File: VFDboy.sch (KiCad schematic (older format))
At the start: 59 parts, among them J1 AVR-ISP-6, SW1 RIGHT, SW2 A, SW3 DOWN, SW4 UP, SW5 LEFT, SW6 B, U1 ATmega32U4-MU, U2 SSD1306_VFD, U7 SRV05-4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

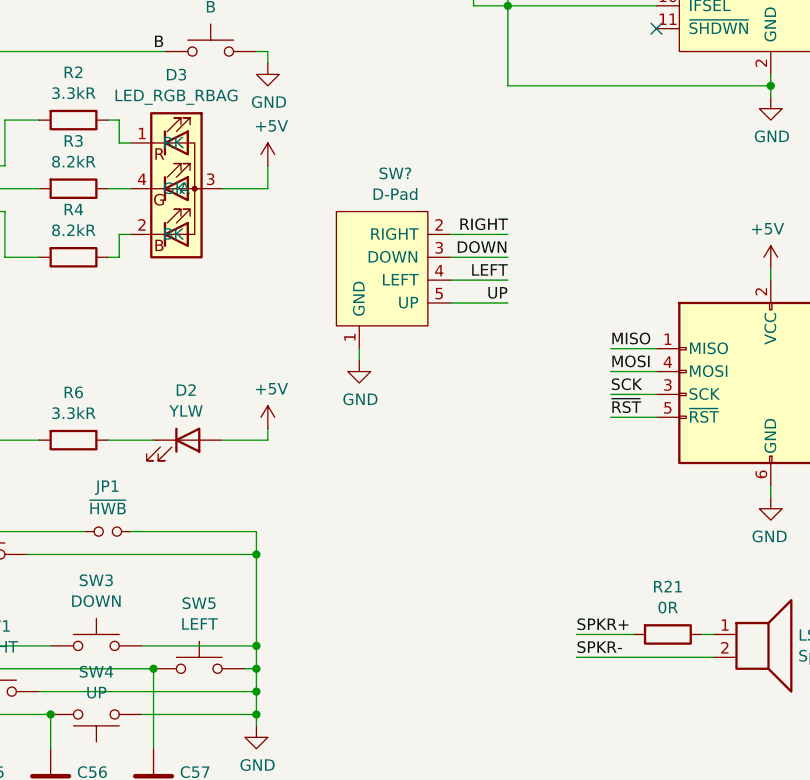
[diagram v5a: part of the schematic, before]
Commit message: Implement elevated AB surfaces
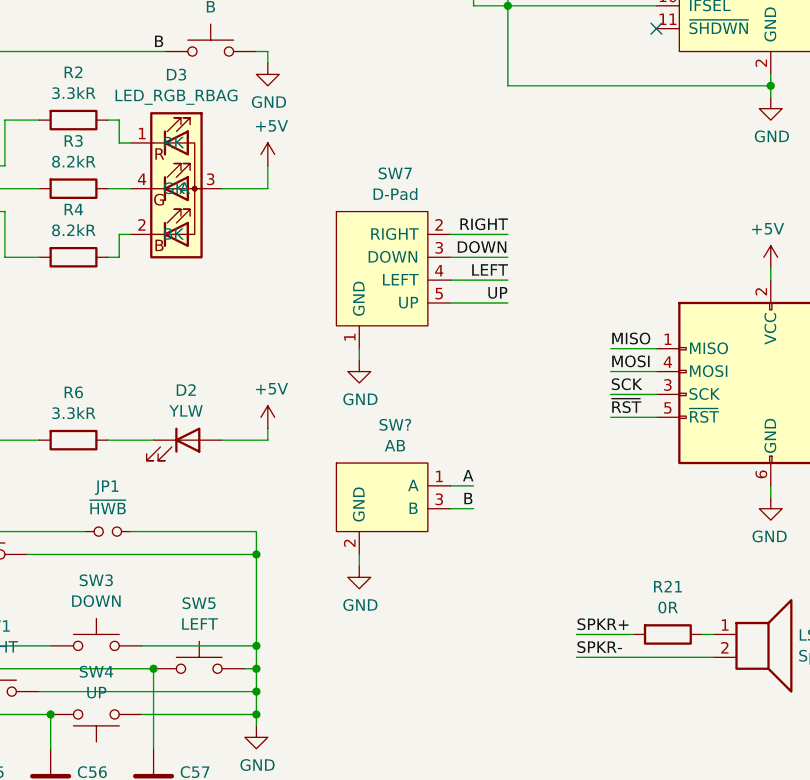
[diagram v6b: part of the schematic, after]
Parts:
- added SW?: AB, button-daughterboard:Daugtherboard_AB, symbol Button_Daughterboard:AB
- gave numbers to parts that had none: 1
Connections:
- net A: now also SW?.1 (A)
- net B: now also SW?.3 (B)
- net GND: now also SW?.2 (GND)
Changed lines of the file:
@@
 	6200 4350 5900 4350
 $Comp
-L Button_Daughterboard:D-Pad SW?
+L Button_Daughterboard:D-Pad SW7
 U 1 1 623C0A73
 P 8500 3100
-F 0 "SW?" H 8558 3515 50  0000 C CNN
+F 0 "SW7" H 8558 3515 50  0000 C CNN
 F 1 "D-Pad" H 8558 3424 50  0000 C CNN
 F 2 "button-daughterboard:Daughterboard_D-Pad" H 8550 2950 50  0001 C CNN
@@
 $EndComp
 $Comp
-L power:GND #PWR?
+L power:GND #PWR0134
 U 1 1 623C143C
 P 8400 3500
-F 0 "#PWR?" H 8400 3250 50  0001 C CNN
+F 0 "#PWR0134" H 8400 3250 50  0001 C CNN
 F 1 "GND" H 8405 3327 50  0000 C CNN
 F 2 "" H 8400 3500 50  0001 C CNN
@@
 Wire Wire Line
 	9050 3250 8800 3250
+$Comp
+L Button_Daughterboard:AB SW?
+U 1 1 6007D848
+P 8500 4100
+F 0 "SW?" H 8558 4415 50  0000 C CNN
+F 1 "AB" H 8558 4324 50  0000 C CNN
+F 2 "button-daughterboard:Daugtherboard_AB" H 8550 4050 50  0001 C CNN
+F 3 "" H 8550 4050 50  0001 C CNN
+	1    8500 4100
+	1    0    0    -1
+$EndComp
+$Comp
+L power:GND #PWR?
+U 1 1 6007E5AC
+P 8400 4400
+F 0 "#PWR?" H 8400 4150 50  0001 C CNN
+F 1 "GND" H 8405 4227 50  0000 C CNN
+F 2 "" H 8400 4400 50  0001 C CNN
+F 3 "" H 8400 4400 50  0001 C CNN
+	1    8400 4400
+	1    0    0    -1
+$EndComp
+Wire Wire Line
+	8400 4400 8400 4350
+Wire Wire Line
+	8800 4050 8900 4050
+Text Label 8900 4050 2    50   ~ 0
+A
+Wire Wire Line
+	8800 4150 8900 4150
+Text Label 8900 4150 2    50   ~ 0
+B
 $EndSCHEMATC

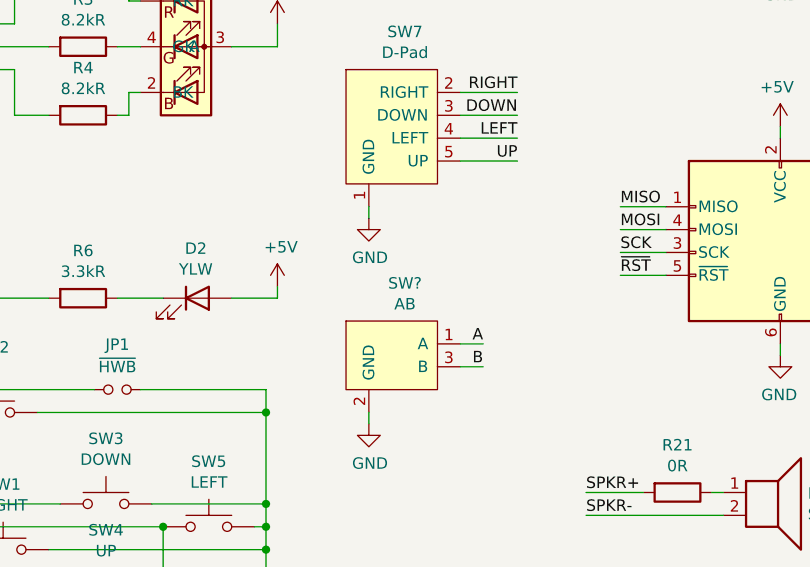
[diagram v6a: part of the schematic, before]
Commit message: Use tactile power switch
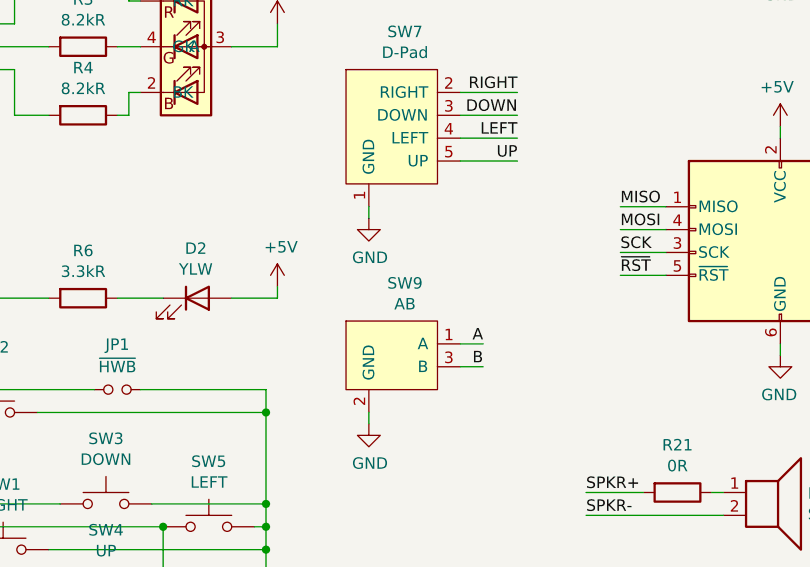
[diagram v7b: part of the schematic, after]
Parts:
- gave numbers to parts that had none: 1
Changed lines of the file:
@@
 	9050 3250 8800 3250
 $Comp
-L Button_Daughterboard:AB SW?
+L Button_Daughterboard:AB SW9
 U 1 1 6007D848
 P 8500 4100
-F 0 "SW?" H 8558 4415 50  0000 C CNN
+F 0 "SW9" H 8558 4415 50  0000 C CNN
 F 1 "AB" H 8558 4324 50  0000 C CNN
 F 2 "button-daughterboard:Daugtherboard_AB" H 8550 4050 50  0001 C CNN
@@
 $EndComp
 $Comp
-L power:GND #PWR?
+L power:GND #PWR0135
 U 1 1 6007E5AC
 P 8400 4400
-F 0 "#PWR?" H 8400 4150 50  0001 C CNN
+F 0 "#PWR0135" H 8400 4150 50  0001 C CNN
 F 1 "GND" H 8405 4227 50  0000 C CNN
 F 2 "" H 8400 4400 50  0001 C CNN

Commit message: Reduce paste coverage on QFN and DFN thermal pads
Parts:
- U1: footprint Package_DFN_QFN:QFN-44-1EP_7x7mm_P0.5mm_EP5.2x5.2mm -> QFN_little_paste:QFN-44-1EP_7x7mm_P0.5mm_EP5.2x5.2mm_little_paste
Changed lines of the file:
@@
 F 0 "U1" H 4950 5400 50  0000 C CNN
 F 1 "ATmega32U4-MU" V 5300 3650 50  0000 C CNN
-F 2 "Package_DFN_QFN:QFN-44-1EP_7x7mm_P0.5mm_EP5.2x5.2mm" H 5300 3650 50  0001 C CIN
+F 2 "QFN_little_paste:QFN-44-1EP_7x7mm_P0.5mm_EP5.2x5.2mm_little_paste" H 5300 3650 50  0001 C CIN
 F 3 "http://ww1.microchip.com/downloads/en/DeviceDoc/Atmel-7766-8-bit-AVR-ATmega16U4-32U4_Datasheet.pdf" H 5300 3650 50  0001 C CNN
 F 4 "C45874" H 5300 3650 50  0001 C CNN "LCSC"
